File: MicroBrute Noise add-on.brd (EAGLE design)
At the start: 16.1 x 25.5 mm, 19 parts, among them IC1 TL071D, Q1 mmbt3904, Q2 mmbt3904, Q3 mmbt3904

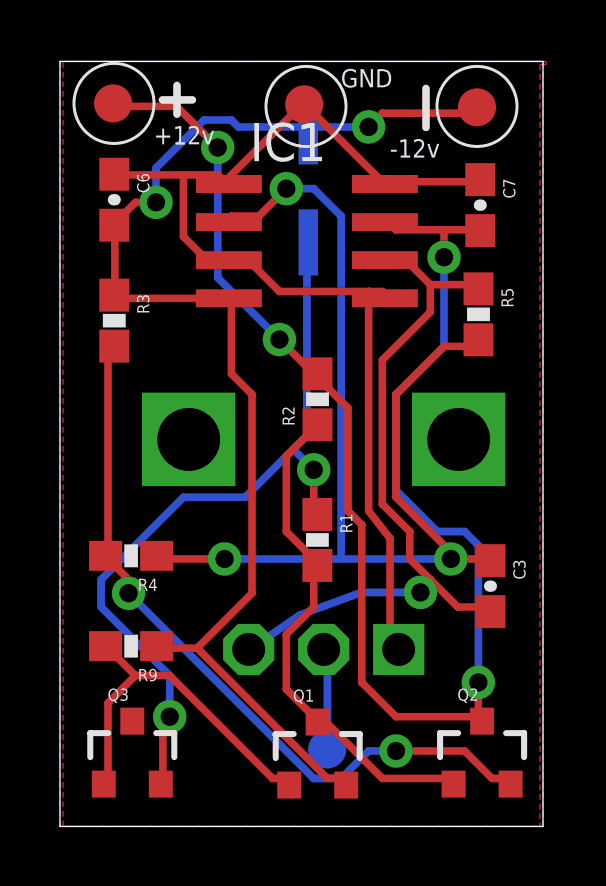
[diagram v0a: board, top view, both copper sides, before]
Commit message: Added diodes to pcb, uploaded BOM
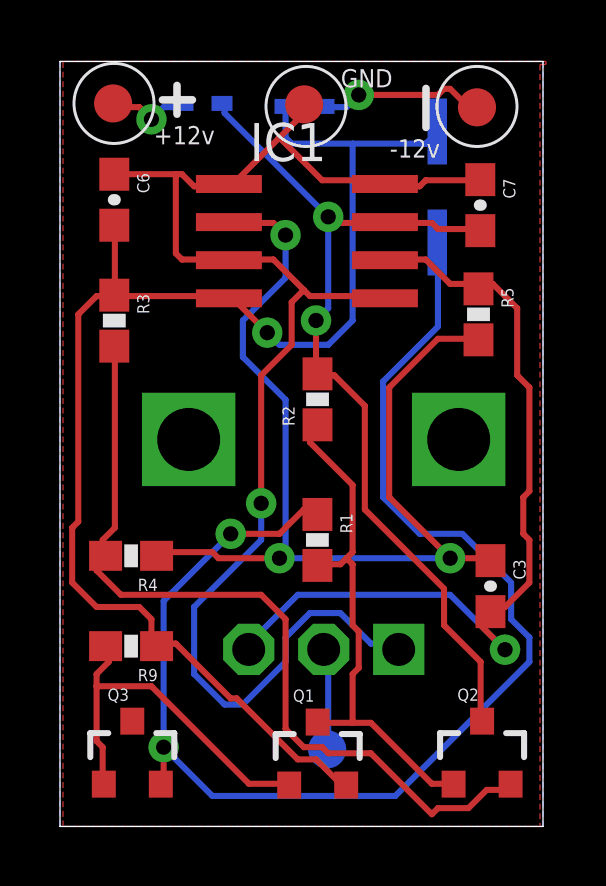
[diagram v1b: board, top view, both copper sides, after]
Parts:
- added D1, D2: PMEG2010AEB, diode:SOD523
- moved C1 4.30 mm to (12.4, 21.4)
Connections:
- new net N$10: -12_VOLT.P$1, D2.C
- new net N$8: +12_VOLT.P$1, D1.A
- net VCC: now also D1.C; no longer +12_VOLT.P$1
- net VEE: now also D2.A; no longer -12_VOLT.P$1
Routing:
- net VCC: track 50.4 -> 30.0 mm, vias 4 -> 2
- net N$3: track 25.7 -> 45.0 mm
- net GND: track 37.4 -> 49.4 mm, vias 0 -> 1
- net N$10: track 0.00 -> 5.82 mm, vias 0 -> 1
- net VEE: track 42.0 -> 46.6 mm, vias 2 -> 1
- net N$6: track 23.9 -> 28.4 mm
- net N$8: track 0.00 -> 2.84 mm, vias 0 -> 1
- net N$4: track 24.9 -> 27.5 mm, vias 2 -> 0
- net N$9: track 37.2 -> 35.5 mm
- net N$2: track 12.1 -> 12.7 mm
